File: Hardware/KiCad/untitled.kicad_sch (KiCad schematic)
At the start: 14 parts, among them U103 ATmega328P-A, Y1 Crystal

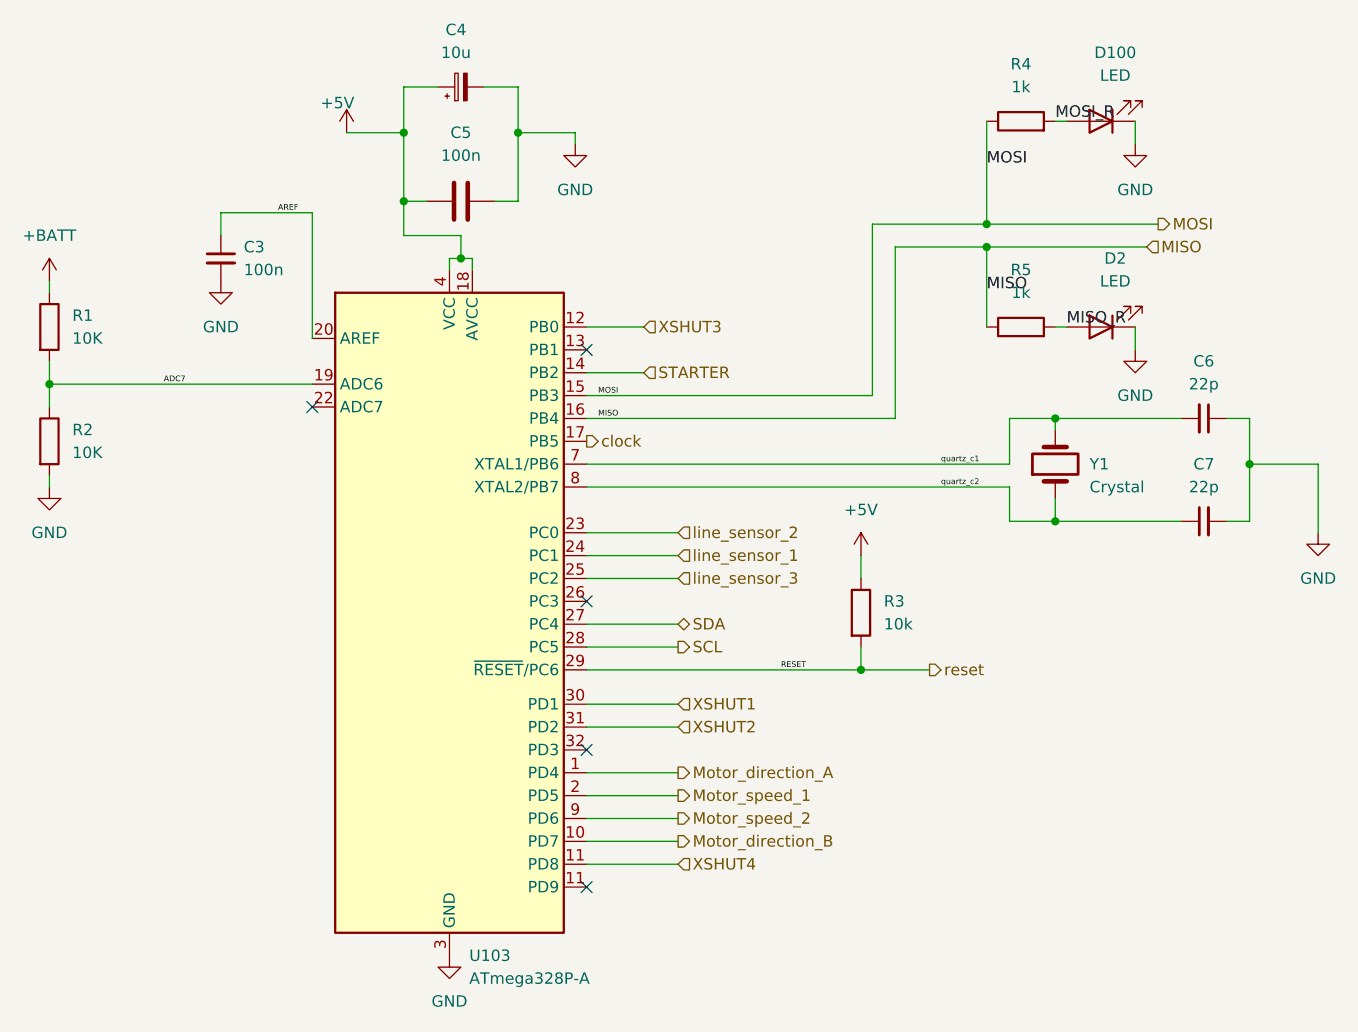
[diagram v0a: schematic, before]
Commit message: change to pinout of atemega for PWM Motor 1
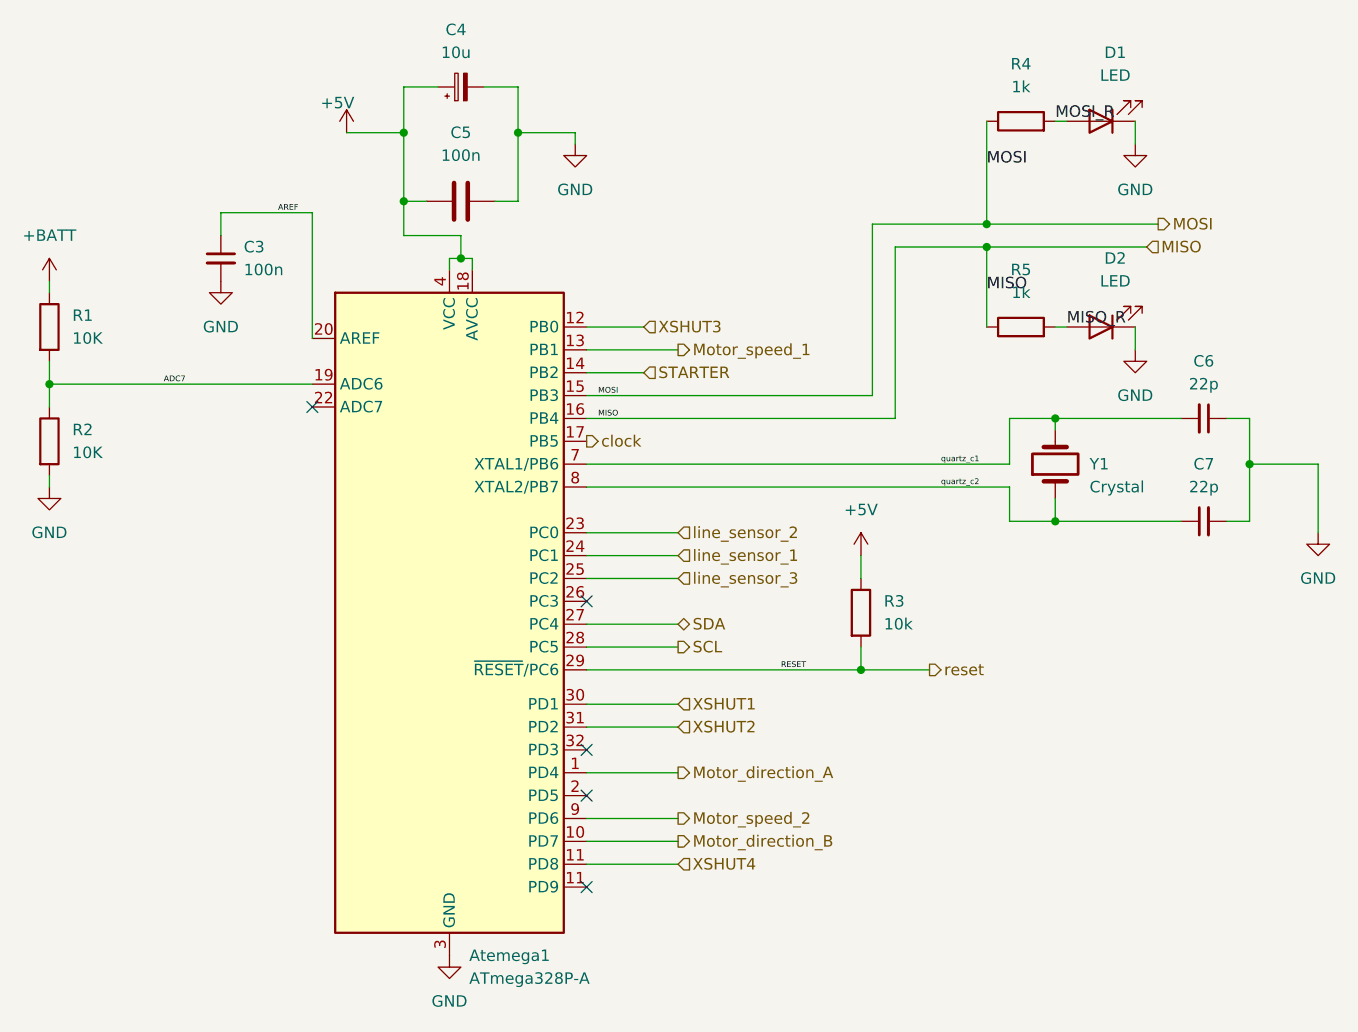
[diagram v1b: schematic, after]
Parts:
- renumbered U103 to Atemega1, D100 to D1
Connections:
- net Motor_speed_1: now also Atemega1.13 (PB1); no longer Atemega1.2 (PD5)
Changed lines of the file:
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@@
 (kicad_sch
-	(version 20231120)
+	(version 20250114)
 	(generator "eeschema")
-	(generator_version "8.0")
+	(generator_version "9.0")
 	(paper "A4")
 	(junction
@@
 	)
 	(no_connect
+		(at 143.51 118.11)
+	)
+	(no_connect
 		(at 143.51 113.03)
 	)
-	(no_connect
-		(at 143.51 68.58)
-	)
 	(wire
 		(pts
@@
 	(wire
 		(pts
-			(xy 143.51 118.11) (xy 153.67 118.11)
+			(xy 143.51 68.58) (xy 153.67 68.58)
 		)
 		(stroke
@@
 	(label "MISO"
 		(at 187.96 62.23 0)
-		(fields_autoplaced yes)
 		(effects
 			(font
@@
 	(label "quartz_c2"
 		(at 182.88 83.82 0)
-		(fields_autoplaced yes)
 		(effects
 			(font
@@
 	(label "MOSI"
 		(at 144.78 73.66 0)
-		(fields_autoplaced yes)
 		(effects
 			(font
@@
 	(label "AREF"
 		(at 109.22 53.34 0)
-		(fields_autoplaced yes)
 		(effects
 			(font
@@
 	(label "MOSI_R"
 		(at 195.58 43.18 0)
-		(fields_autoplaced yes)
 		(effects
 			(font
@@
 	(label "RESET"
 		(at 165.1 104.14 0)
-		(fields_autoplaced yes)
 		(effects
 			(font
@@
 	(label "MISO"
 		(at 144.78 76.2 0)
-		(fields_autoplaced yes)
 		(effects
 			(font
@@
 	(label "MISO_R"
 		(at 196.85 66.04 0)
-		(fields_autoplaced yes)
 		(effects
 			(font
@@
 	(label "quartz_c1"
 		(at 182.88 81.28 0)
-		(fields_autoplaced yes)
 		(effects
 			(font
@@
 	(label "ADC7"
 		(at 96.52 72.39 0)
-		(fields_autoplaced yes)
 		(effects
 			(font
@@
 	(label "MOSI"
 		(at 187.96 48.26 0)
-		(fields_autoplaced yes)
 		(effects
 			(font
@@
 		(shape input)
 		(at 153.67 125.73 0)
-		(fields_autoplaced yes)
 		(effects
 			(font
@@
 		(shape input)
 		(at 153.67 107.95 0)
-		(fields_autoplaced yes)
 		(effects
 			(font
@@
 		(shape output)
 		(at 153.67 115.57 0)
-		(fields_autoplaced yes)
 		(effects
 			(font
@@
 		(shape input)
 		(at 153.67 110.49 0)
-		(fields_autoplaced yes)
 		(effects
 			(font
@@
 		(shape bidirectional)
 		(at 153.67 99.06 0)
-		(fields_autoplaced yes)
 		(effects
 			(font
@@
 		(shape output)
 		(at 153.67 123.19 0)
-		(fields_autoplaced yes)
 		(effects
 			(font
@@
 		(shape input)
 		(at 205.74 57.15 0)
-		(fields_autoplaced yes)
 		(effects
 			(font
@@
 		(shape output)
 		(at 153.67 101.6 0)
-		(fields_autoplaced yes)
 		(effects
 			(font
@@
 		(shape input)
 		(at 153.67 93.98 0)
-		(fields_autoplaced yes)
 		(effects
 			(font
@@
 		(shape input)
 		(at 153.67 88.9 0)
-		(fields_autoplaced yes)
 		(effects
 			(font
@@
 		(shape output)
 		(at 207.01 54.61 0)
-		(fields_autoplaced yes)
 		(effects
 			(font
@@
 		(shape input)
 		(at 149.86 71.12 0)
-		(fields_autoplaced yes)
-		(effects
-			(font
-				(size 1.27 1.27)
-			)
-			(justify left)
-		)
-	)
-	(hierarchical_label "Motor_speed_1"
-		(shape output)
-		(at 153.67 118.11 0)
-		(fields_autoplaced yes)
 		(effects
 			(font
@@
 		(shape output)
 		(at 143.51 78.74 0)
-		(fields_autoplaced yes)
 		(effects
 			(font
@@
 		(shape output)
 		(at 153.67 120.65 0)
-		(fields_autoplaced yes)
 		(effects
 			(font
@@
 		(shape output)
 		(at 181.61 104.14 0)
-		(fields_autoplaced yes)
+		(effects
+			(font
+				(size 1.27 1.27)
+			)
+			(justify left)
+		)
+	)
+	(hierarchical_label "Motor_speed_1"
+		(shape output)
+		(at 153.67 68.58 0)
 		(effects
 			(font
@@
 		(shape input)
 		(at 153.67 91.44 0)
-		(fields_autoplaced yes)
 		(effects
 			(font
@@
 		(shape input)
 		(at 149.86 66.04 0)
-		(fields_autoplaced yes)
 		(effects
 			(font
@@
 		(on_board yes)
 		(dnp no)
-		(property "Reference" "#PWR01"
+		(property "Reference" "#PWR032"
 			(at 116.84 48.26 0)
 			(effects
@@
 		(dnp no)
 		(fields_autoplaced yes)
-		(property "Reference" "U103"
+		(property "Reference" "Atemega1"
 			(at 130.4641 135.89 0)
 			(effects
@@
 		(dnp no)
 		(fields_autoplaced yes)
-		(property "Reference" "D100"
+		(property "Reference" "D1"
 			(at 202.2475 35.56 0)
 			(effects
@@
 		(dnp no)
 		(fields_autoplaced yes)
-		(property "Reference" "#PWR0102"
+		(property "Reference" "#PWR033"
 			(at 128.27 142.24 0)
 			(effects
